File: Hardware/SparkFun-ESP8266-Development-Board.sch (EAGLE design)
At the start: 72 parts, among them J1 DNP, Q1 2.5A/30V, U1 ESP8266, U2 MCP73831, U3 AT25SF041-SOIC8, U4 AP2112K-3.3V, U5 ATECC108-MAHDA, U6 TMP1021:1, U7 TSL2561FN, Y1 26MHz

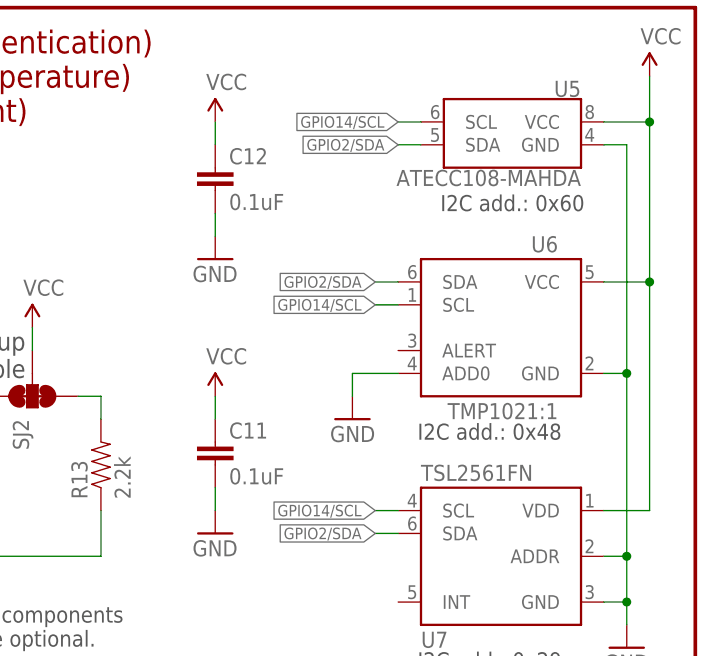
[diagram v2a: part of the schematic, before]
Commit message: Revising TMP102, ATECC108 & TSL2561 to DNP. Moving dimensions to correct layer.
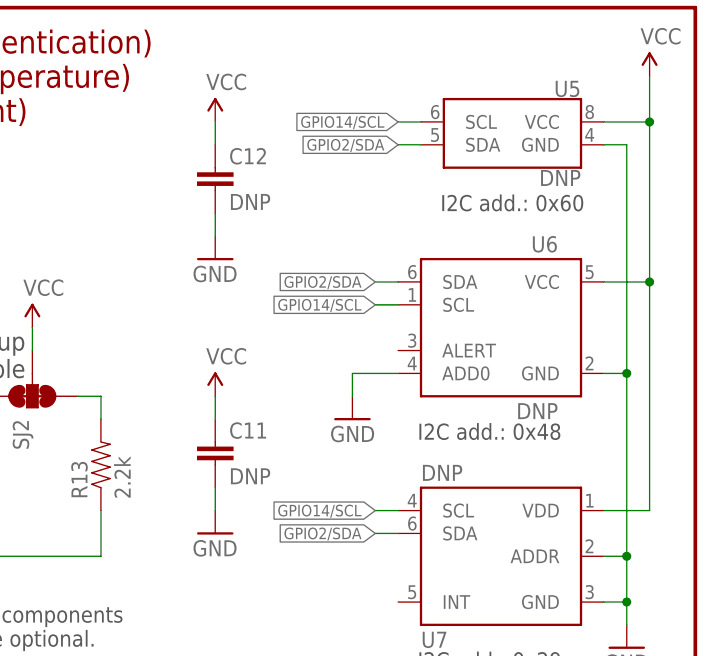
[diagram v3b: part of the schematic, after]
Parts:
- C11, C12: value 0.1uF -> DNP
- U5: value ATECC108-MAHDA -> DNP
- U6: value TMP1021:1 -> DNP
- U7: value TSL2561FN -> DNP
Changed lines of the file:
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@@
 <part name="GND20" library="SparkFun-Aesthetics" deviceset="GND" device=""/>
 <part name="U3" library="esp8266-development-board" deviceset="AT25SF041" device="-SOIC8"/>
-<part name="U5" library="esp8266-development-board" deviceset="ATECC108" device="-MAHDA" value="ATECC108-MAHDA"/>
+<part name="U5" library="esp8266-development-board" deviceset="ATECC108" device="-MAHDA" value="DNP"/>
 <part name="SUPPLY13" library="SparkFun-Aesthetics" deviceset="VCC" device=""/>
 <part name="R13" library="SparkFun-Resistors" deviceset="2.2KOHM1/10W1%(0603)" device="" value="2.2k"/>
@@
 </part>
 <part name="C10" library="SparkFun-Capacitors" deviceset="0.1UF-25V(+80/-20%)(0603)" device="" value="0.1uF"/>
-<part name="C11" library="SparkFun-Capacitors" deviceset="0.1UF-25V(+80/-20%)(0603)" device="" value="0.1uF"/>
+<part name="C11" library="SparkFun-Capacitors" deviceset="0.1UF-25V(+80/-20%)(0603)" device="" value="DNP"/>
 <part name="Q1" library="SparkFun-DiscreteSemi" deviceset="MOSFET-PCHANNEL" device="DMG2307L" value="2.5A/30V"/>
 <part name="R16" library="SparkFun-Resistors" deviceset="200OHM1/10W1%(0603)" device="" value="200"/>
@@
 <part name="R17" library="SparkFun-Resistors" deviceset="10KOHM1/10W1%(0603)" device="0603" value="10K"/>
 <part name="GND28" library="SparkFun-Aesthetics" deviceset="GND" device=""/>
-<part name="U6" library="SparkFun-Sensors" deviceset="TMP102" device="1:1"/>
+<part name="U6" library="SparkFun-Sensors" deviceset="TMP102" device="1:1" value="DNP"/>
 <part name="GND30" library="SparkFun-Aesthetics" deviceset="GND" device=""/>
 <part name="SUPPLY11" library="SparkFun-Aesthetics" deviceset="VCC" device=""/>
@@
 <part name="SUPPLY12" library="SparkFun-Aesthetics" deviceset="VIN" device=""/>
 <part name="GND24" library="SparkFun-Aesthetics" deviceset="GND" device=""/>
-<part name="U7" library="esp8266-development-board" deviceset="TSL2561" device="FN"/>
+<part name="U7" library="esp8266-development-board" deviceset="TSL2561" device="FN" value="DNP"/>
 <part name="GND31" library="SparkFun-Aesthetics" deviceset="GND" device=""/>
 <part name="SUPPLY17" library="SparkFun-Aesthetics" deviceset="VCC" device=""/>
 <part name="GND32" library="SparkFun-Aesthetics" deviceset="GND" device=""/>
-<part name="C12" library="SparkFun-Capacitors" deviceset="0.1UF-25V(+80/-20%)(0603)" device="" value="0.1uF"/>
+<part name="C12" library="SparkFun-Capacitors" deviceset="0.1UF-25V(+80/-20%)(0603)" device="" value="DNP"/>
 <part name="SUPPLY15" library="SparkFun-Aesthetics" deviceset="VCC" device=""/>
 <part name="GND25" library="SparkFun-Aesthetics" deviceset="GND" device=""/>
